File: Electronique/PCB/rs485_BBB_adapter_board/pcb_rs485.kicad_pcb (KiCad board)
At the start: 2 copper layers, 63.5 x 43.2 mm, 9 parts, among them J1 Conn_01x03_Male, J2 Conn_01x02_Male, J3 Conn_01x02_Male, U1 D0010, U2 MAX485

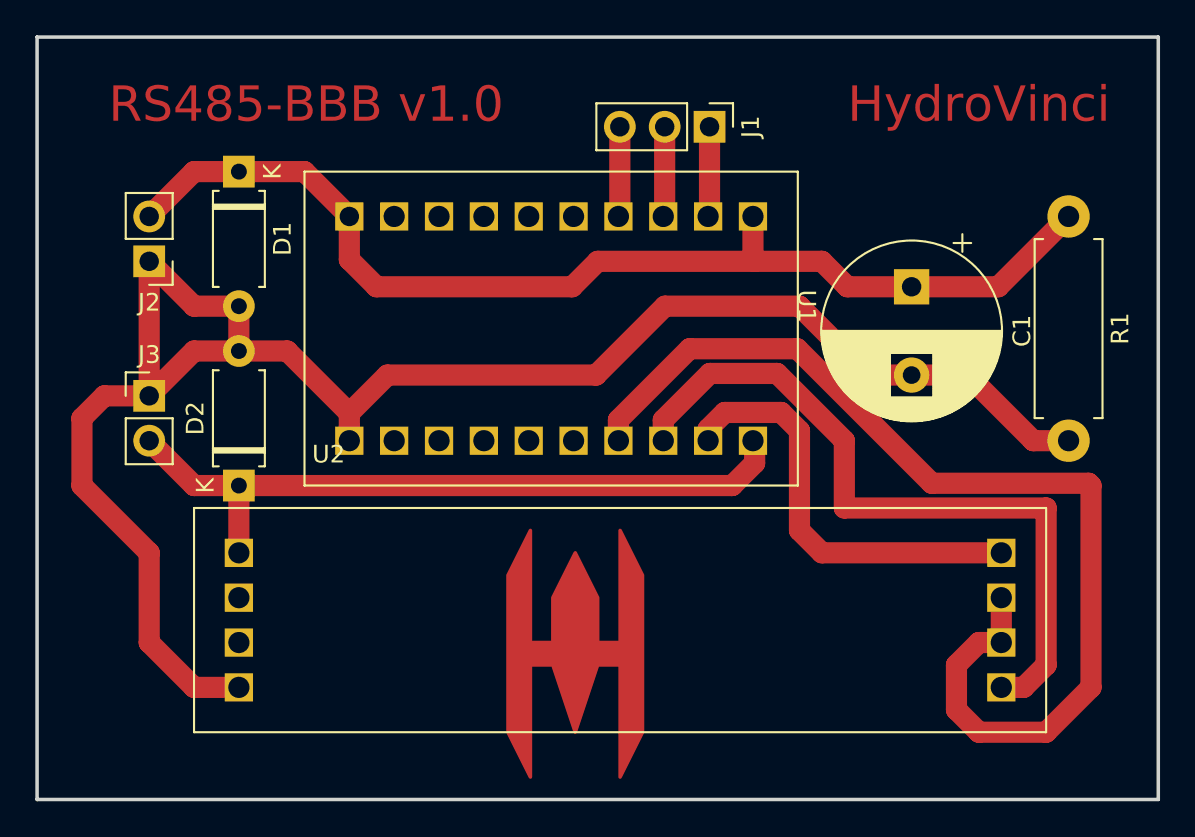
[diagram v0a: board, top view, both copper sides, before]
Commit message: update to pcb for environnement sensors + external libs
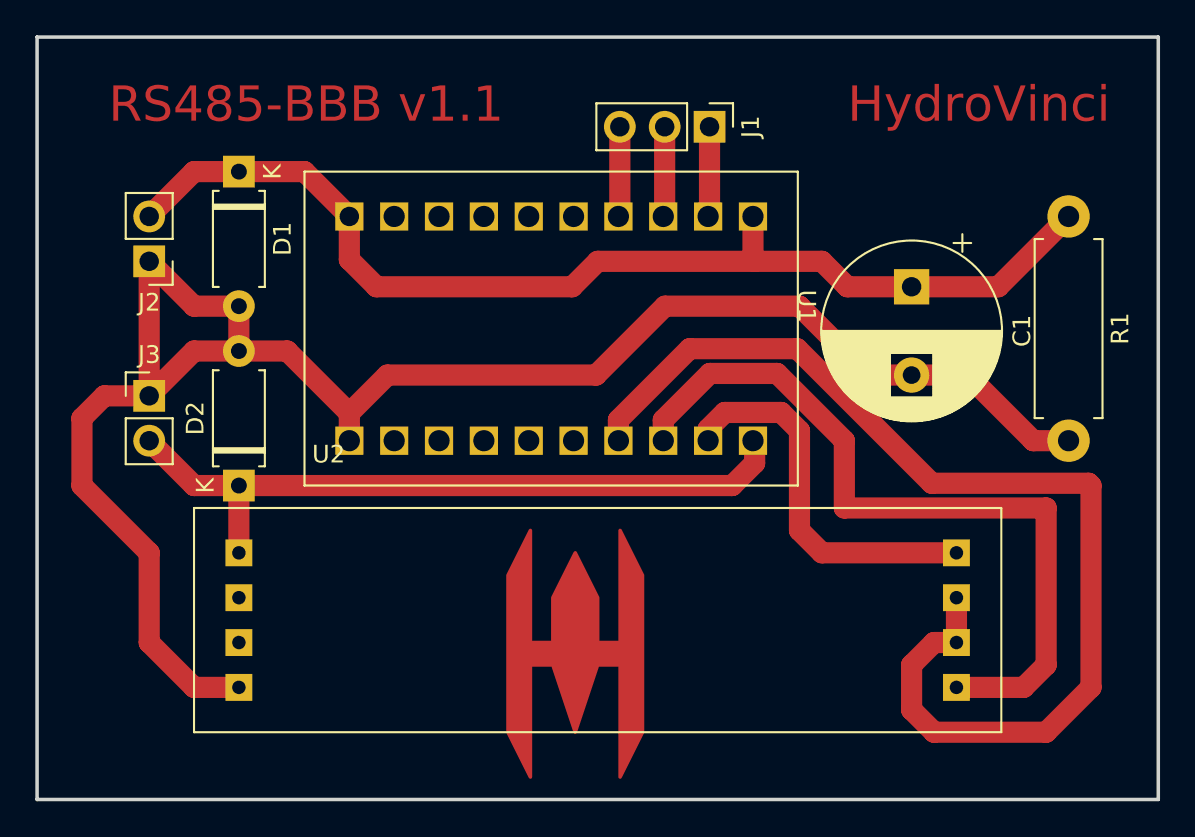
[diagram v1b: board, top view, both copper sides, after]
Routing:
- net /RX: track 41.3 -> 43.8 mm
- net /TX: track 24.3 -> 21.7 mm
- net /ENABLE: track 61.6 -> 64.1 mm
- added copper zone on F.Cu, net GND
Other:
- board text added: "RS485-BBB v1.1"
- board text removed: "RS485-BBB v1.0"
